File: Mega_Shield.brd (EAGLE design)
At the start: 91.4 x 53.3 mm, 21 parts, among them IC1 MPL3115A2LGA, U1 USD-SOCKETNEW, U2 74HC4050, U4 FGPMMOPA6H, X1 22-23-2021

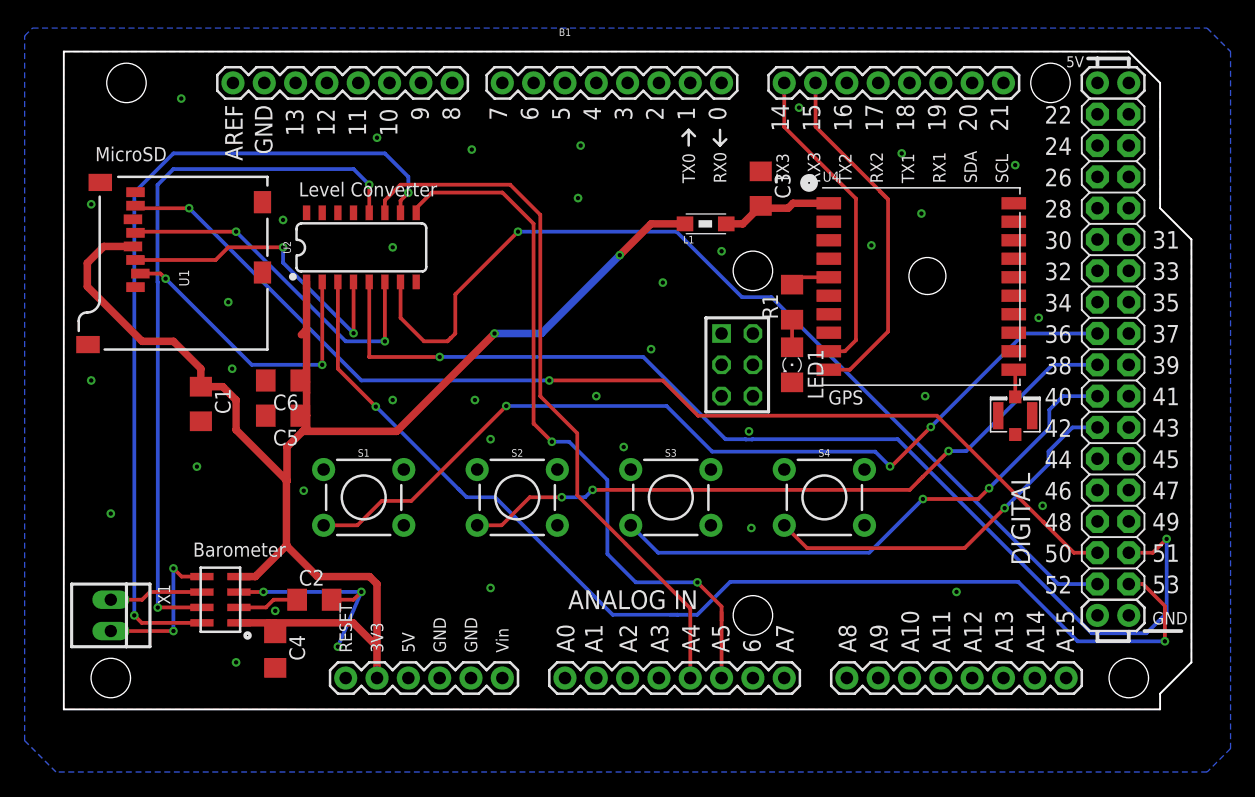
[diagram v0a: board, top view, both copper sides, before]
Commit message: Rev 0.2
Uno edition
Mega edition

Individual switches (cheaper, replacable!)
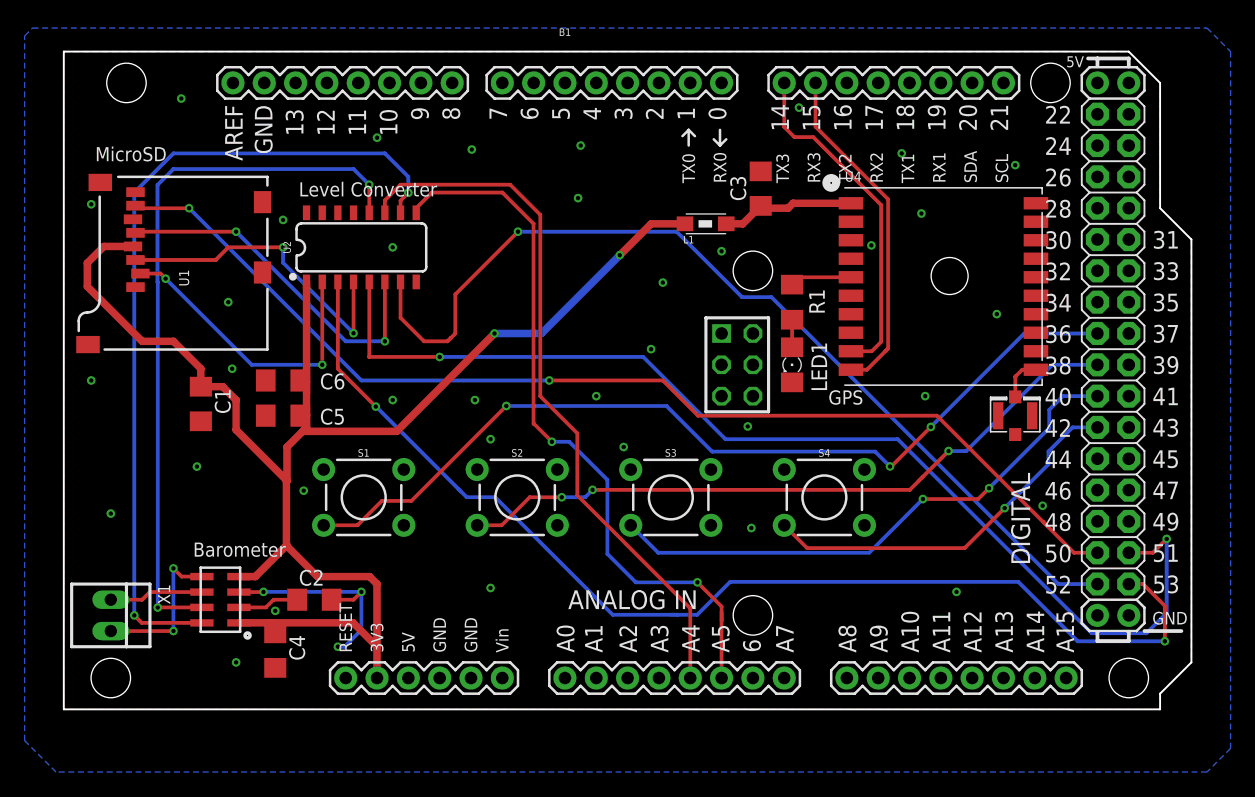
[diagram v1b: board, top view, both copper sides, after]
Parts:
- moved U4 1.80 mm to (79.0, 34.3)
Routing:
- net TX3: track 25.8 -> 28.4 mm
- net 3D-FIX: track 3.23 -> 5.03 mm
- net RX3: track 29.4 -> 28.0 mm
- net 3V3_CLEAN: track 9.69 -> 11.1 mm
- net EX_ANT: track 2.25 -> 3.62 mm
- net GND: track 17.4 -> 18.2 mm
- net 3.3V: track 127.2 -> 126.6 mm
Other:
- board text added: "Surveyor 0.2 Arduino Mega Adam Rankin https://github.com/adamrankin/SurveyorShield"
- board text removed: "Surveyor 0.1 Adam Rankin https://github.com/adamrankin/SurveyorShield"
